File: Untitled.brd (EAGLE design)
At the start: 45.7 x 45.7 mm, 34 parts, among them IC1 ILD4001, IC2 ILD4001, IC3 ILD4001, Q1 BSS138, Q2 BSS138, U1 ATMEGA328P

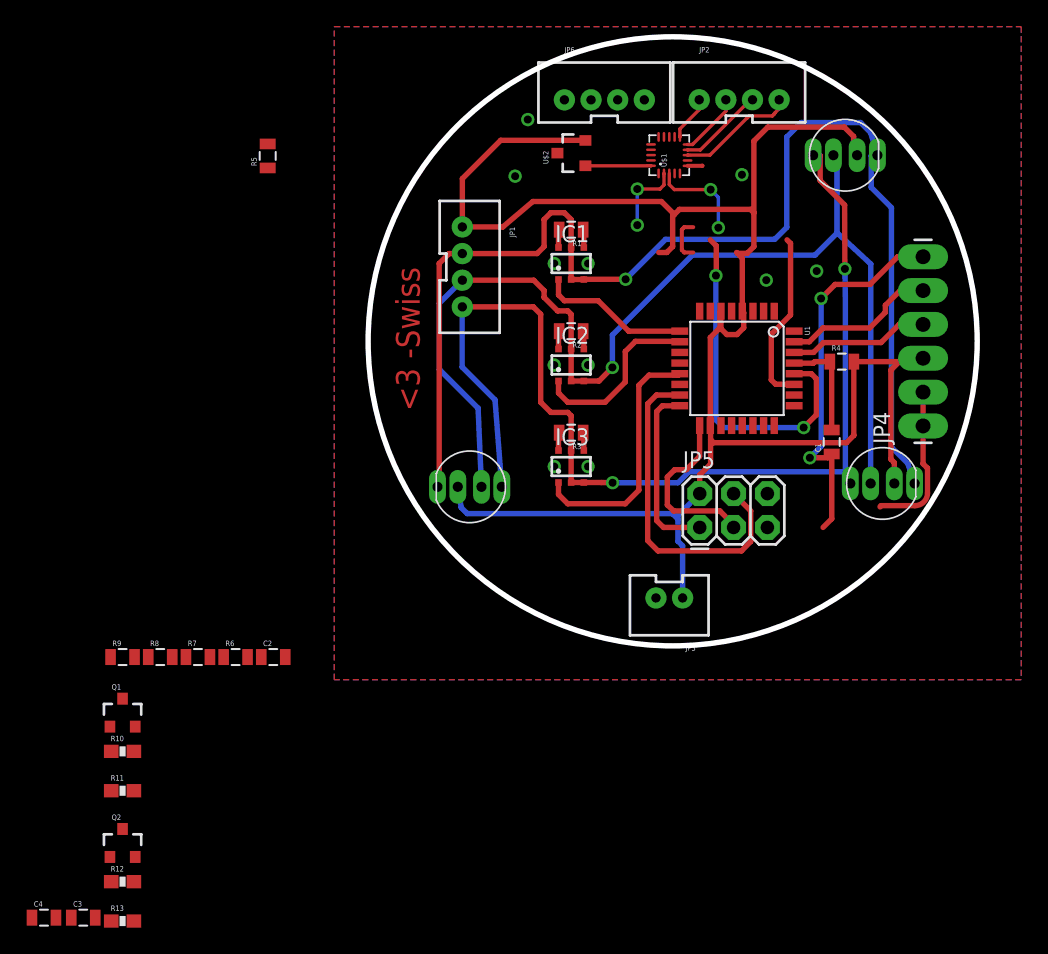
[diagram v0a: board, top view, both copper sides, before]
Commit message: Added resistors
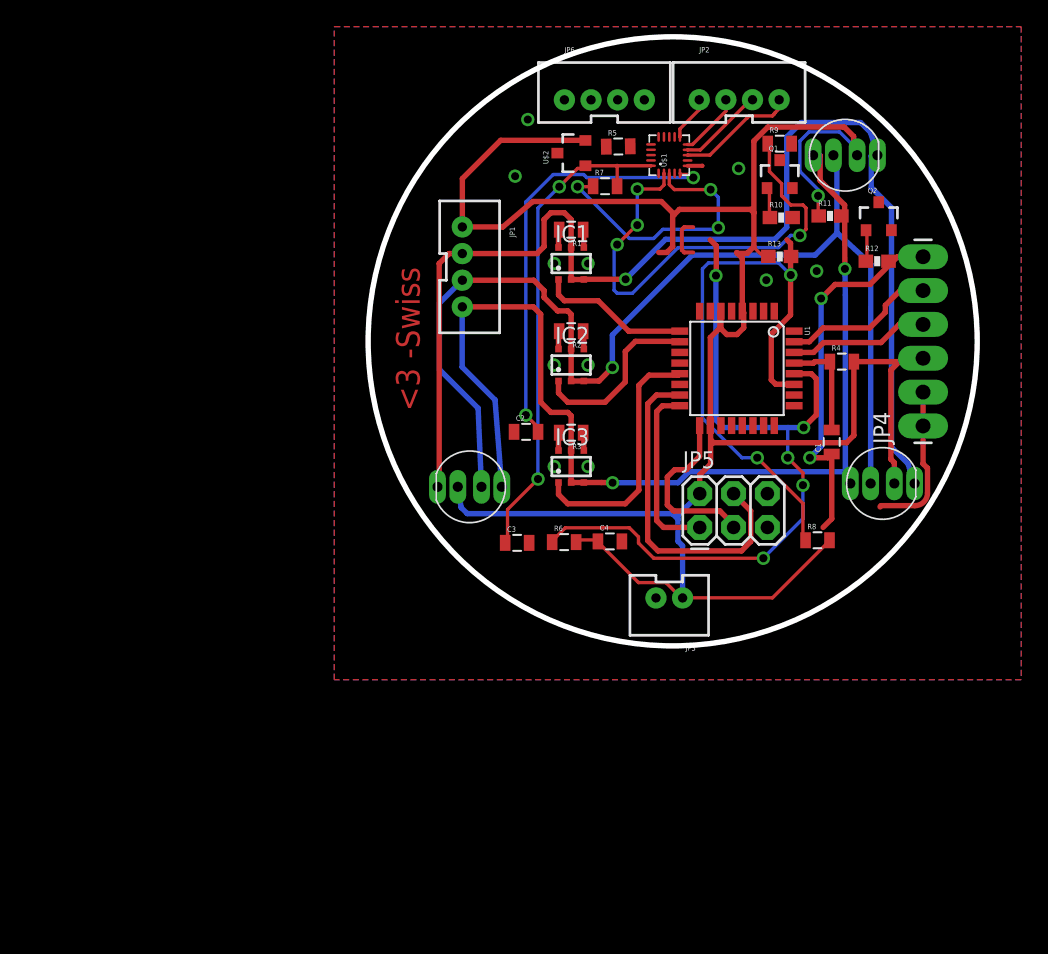
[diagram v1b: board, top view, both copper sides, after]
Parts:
- moved Q2 73.7 mm to (66.3, 60.1)
- moved R12 73.3 mm to (66.2, 56.8)
- moved R13 70.2 mm to (58.8, 57.2)
- moved R11 68.4 mm to (62.6, 60.2)
- moved Q1 63.8 mm to (58.8, 63.3)
- moved R10 63.6 mm to (59.0, 60.1)
- moved R9 62.6 mm to (58.8, 65.6)
- moved C4 51.0 mm to (46.1, 35.8)
- moved R8 50.1 mm to (61.7, 35.9)
- moved R7 46.7 mm to (45.7, 62.4)
- moved C3 43.0 mm to (39.1, 35.7)
- moved R5 26.3 mm to (46.7, 65.4), turned to 0.8 degrees
- moved R6 26.1 mm to (42.7, 35.7)
- moved C2 25.4 mm to (39.8, 44.0)
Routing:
- net 3V: track 4.92 -> 42.2 mm, vias 0 -> 2
- net VCC: track 142.2 -> 178.1 mm, vias 0 -> 1
- net N$17: track 0.00 -> 32.5 mm, vias 0 -> 2
- net SDA: track 13.1 -> 44.6 mm, vias 0 -> 2
- net SCLO: track 5.92 -> 36.2 mm, vias 2 -> 4
- net SCL: track 26.7 -> 55.7 mm, vias 2 -> 5
- net SDAO: track 7.26 -> 21.0 mm, vias 2 -> 3

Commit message: changed level shifter
changed the 5v -> 3v level shifters out for mossiest and changed the
board to support them.
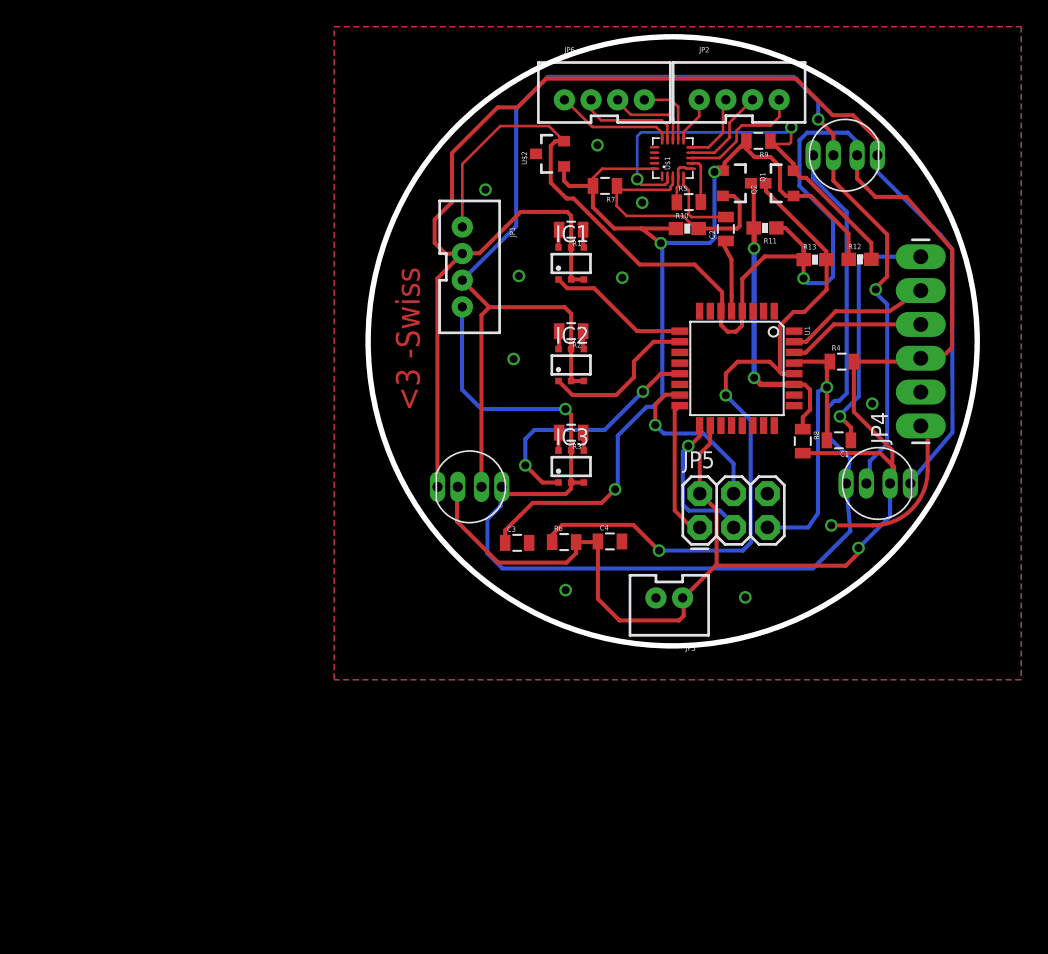
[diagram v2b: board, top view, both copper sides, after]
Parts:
- moved C2 21.4 mm to (54.8, 59.2), turned to 90 degrees
- moved Q2 7.81 mm to (58.9, 62.7), turned to 90 degrees
- moved R8 7.52 mm to (60.6, 43.3), turned to 270 degrees
- moved R10 7.10 mm to (51.9, 59.3)
- moved R5 6.74 mm to (52.0, 61.2)
- moved R11 4.96 mm to (57.7, 59.3), turned to 180 degrees
- moved Q1 3.33 mm to (55.6, 62.7), turned to 270 degrees
- moved R13 2.66 mm to (61.5, 56.9)
- moved R9 1.61 mm to (57.2, 65.9), turned to 180 degrees
- moved U$2 1.61 mm to (41.6, 64.9)
- moved R12 1.29 mm to (64.9, 57.0)
- moved C1 0.55 mm to (63.3, 43.4), turned to 180 degrees
- moved U$1 0.34 mm to (50.8, 64.6)
- moved D2 0.32 mm to (66.2, 40.1)
- moved JP4 0.17 mm to (69.4, 44.5)
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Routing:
- net 3V: track 42.2 -> 76.6 mm, vias 2 -> 3
- net N$17: track 32.5 -> 5.90 mm, vias 2 -> 0
- net SDA: track 44.6 -> 22.5 mm
- net GOUT: track 84.0 -> 100.2 mm, vias 1 -> 2
- net RESET_ISP: track 7.92 -> 23.0 mm, vias 0 -> 1
- net ROUT: track 93.9 -> 108.7 mm, vias 1 -> 0
- net MOSI: track 25.4 -> 13.0 mm, vias 0 -> 1
- net BOUT: track 81.9 -> 92.4 mm, vias 2 -> 1
- net RESET: track 28.8 -> 19.6 mm, vias 2 -> 1
- net N$14: track 0.00 -> 8.88 mm
- net N$13: track 0.00 -> 8.04 mm
- net N$6: track 0.00 -> 6.39 mm
- net GND: track 16.2 -> 21.6 mm, vias 11 -> 10
- net N$5: track 0.00 -> 5.23 mm
- net N$16: track 0.00 -> 3.53 mm
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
